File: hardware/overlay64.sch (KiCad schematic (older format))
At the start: 15 parts, among them IC1 ATMEGA8-P, P1 VIDEO IN, P2 VIDEO OUT, Q1 PNP, U1 LM1881, Y1 14.7456MHz

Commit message: Hardware: Schematics switched to 1284P including USB, still drafting...
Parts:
- removed IC1: ATMEGA8-P, DIL28, symbol ATMEGA8-P
- removed Q1: PNP, symbol Q_PNP_BCE
- removed R1: 4k7, symbol R_Small
- removed RV1: 1K, symbol POT
- added D1, D2: 3.6V, symbol ZENERsmall
- added IC1: ATMEGA1284-P, DIL40, symbol ATMEGA1284-P
- added P3: CHROMA IN, symbol CONN_01X02
- added P4: USB, symbol CONN_01X05
- added P5: CHROMA OUT, symbol CONN_01X02
- added P6: PORTA, symbol CONN_01X08
- added P7: PORTB, symbol CONN_01X08
- added P8: PORTC, symbol CONN_01X08
- added Q? (x2): NPN, symbol Q_NPN_BCE
- added R1, R3: 1k, symbol R
- added R4: 1k5, symbol R
- added R5, R6: 68, symbol R
- P1: value VIDEO IN -> LUMA IN
- P2: value VIDEO OUT -> LUMA OUT
- Y1: value 14.7456MHz -> 16MHz
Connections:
- net labels added: LUMA, OUT, PA0, PA1, PA2, PA3, PA4, PA5, PA6, PA7, PB0, PB1, PB2, PB3, PB4, PB5, PB6, PB7, PC0, PC1, PC2, PC3, PC4, PC5, PC6, PC7
- wire segments 26 -> 22
- no-connect marks 18 -> 8
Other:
- moved on the sheet: C3, C5, C6, R2, U1, Y1

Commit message: Hardware: Switched to atmega32p, updated to current state on breadboard
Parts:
- removed C1, C2: 18pF, symbol CP_Small
- removed D1, D2: 3.6V, symbol ZENERsmall
- removed IC1: ATMEGA1284-P, DIL40, symbol ATMEGA1284-P
- removed P3: CHROMA IN, symbol CONN_01X02
- removed P4: USB, symbol CONN_01X05
- removed P5: CHROMA OUT, symbol CONN_01X02
- removed P6: PORTA, symbol CONN_01X08
- removed P7: PORTB, symbol CONN_01X08
- removed P8: PORTC, symbol CONN_01X08
- removed Q?: NPN, symbol Q_NPN_BCE
- removed R1, R3: 1k, symbol R
- removed R4: 1k5, symbol R
- removed R5, R6: 68, symbol R
- added C1, C2: 18pF, symbol C_Small
- added IC1: ATMEGA328P-P, DIL28, symbol ATMEGA328P-P
- added P1: ISP, symbol CONN_02X03
- added RV1: 1k, symbol POT
- gave numbers to parts that had none: 1
- renumbered C5 to C3, C3 to C5, P1 to P2, P2 to P3, R2 to R1
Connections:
- net labels added: MISO, MOSI, SCK, ~RESET
- net labels removed: LUMA, OUT, PA0, PA1, PA2, PA3, PA4, PA5, PA6, PA7, PB0, PB1, PB2, PB3, PB4, PB5, PB6, PB7, PC0, PC1, PC2, PC3, PC4, PC5, PC6, PC7
- no-connect marks 8 -> 19
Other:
- moved on the sheet: C3, C5, C6, Q1, R1, U1, Y1

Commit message: Hardware: Added vic sockets, layed out components (rough draft)
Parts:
- removed C4: 10uF, symbol CP
- removed P2: LUMA IN, symbol CONN_01X02
- removed P3: LUMA OUT, symbol CONN_01X02
- added C4: 100nF, Capacitors_ThroughHole:C_Disc_D3_P2.5, symbol C
- added P2: VIC IN, Housings_DIP:DIP-40_W15.24mm, symbol CONN_01X40
- added P3: VIC OUT, Housings_DIP:DIP-40_W15.24mm, symbol CONN_01X40
- C1, C2, C3, C5, C6: footprint (none) -> Capacitors_ThroughHole:C_Disc_D3_P2.5
- IC1: footprint DIL28 -> Housings_DIP:DIP-28_W7.62mm
- P1: footprint (none) -> Pin_Headers:Pin_Header_Straight_2x03
- Q1: footprint (none) -> TO_SOT_Packages_THT:TO-92_Inline_Narrow_Oval
- R1: footprint (none) -> Discret:R1
- RV1: footprint (none) -> Potentiometers:Potentiometer_Bourns_3339H_Angular_ScrewUp
- U1: footprint (none) -> Housings_DIP:DIP-8_W7.62mm
- Y1: footprint (none) -> Crystals:Crystal_HC49-U_Vertical
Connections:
- net labels added: LUMA
- wire segments 22 -> 62
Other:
- moved on the sheet: C1, C2, C3, C5, C6, IC1, P1, Q1, R1, RV1, U1, Y1

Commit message: Hardware: Removed VIC-Sockets and pcb layout
Designing this as a VIC-Adpater-board is too complicated, and maybe
not possible (depending on what the modulator still does to the signal
to make it a proper C/Y signal).

It's probably simpler to get LUMA from the connector internally.
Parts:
- removed P2: VIC IN, Housings_DIP:DIP-40_W15.24mm, symbol CONN_01X40
- removed P3: VIC OUT, Housings_DIP:DIP-40_W15.24mm, symbol CONN_01X40
- added P2: MAIN, Pin_Headers:Pin_Header_Straight_1x03, symbol CONN_01X03
- added P3: INPUT, Pin_Headers:Pin_Header_Straight_1x14, symbol CONN_01X14
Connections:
- net labels added: IN0, IN1, IN10, IN11, IN12, IN13, IN2, IN3, IN4, IN5, IN6, IN7, IN8, IN9
- net labels removed: LUMA
- wire segments 62 -> 25
- no-connect marks 19 -> 6
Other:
- moved on the sheet: C4

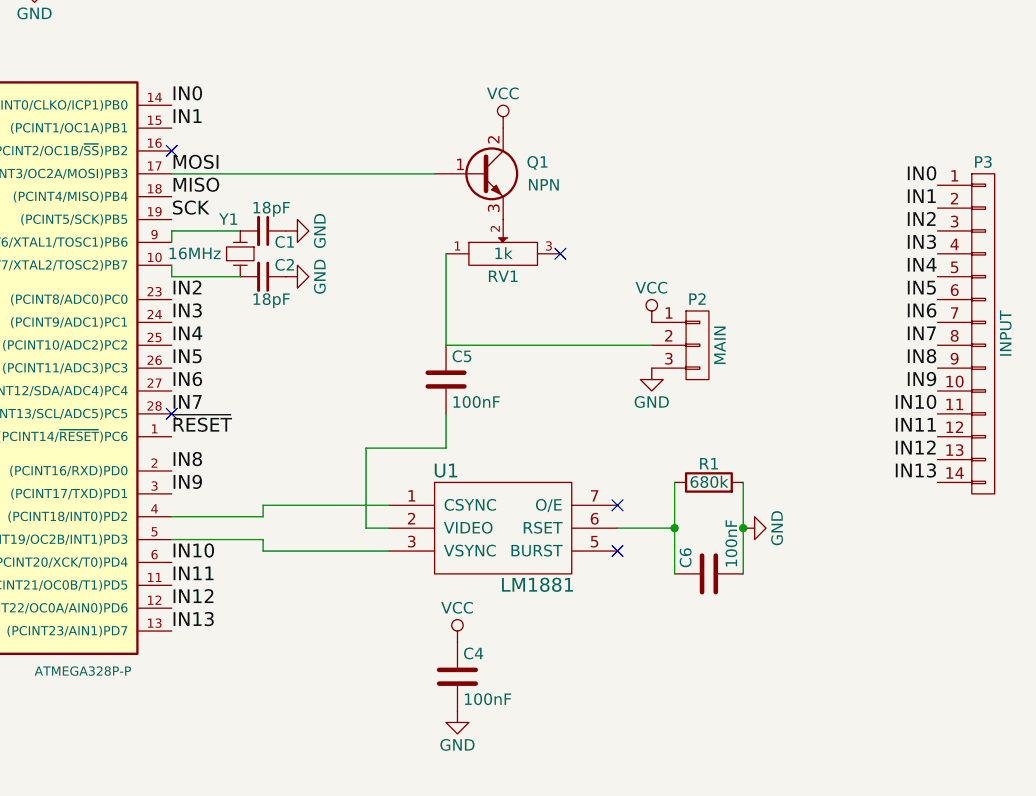
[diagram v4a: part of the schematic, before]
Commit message: Hardware: Updated schematics, Added /OE, resistor before transistor base
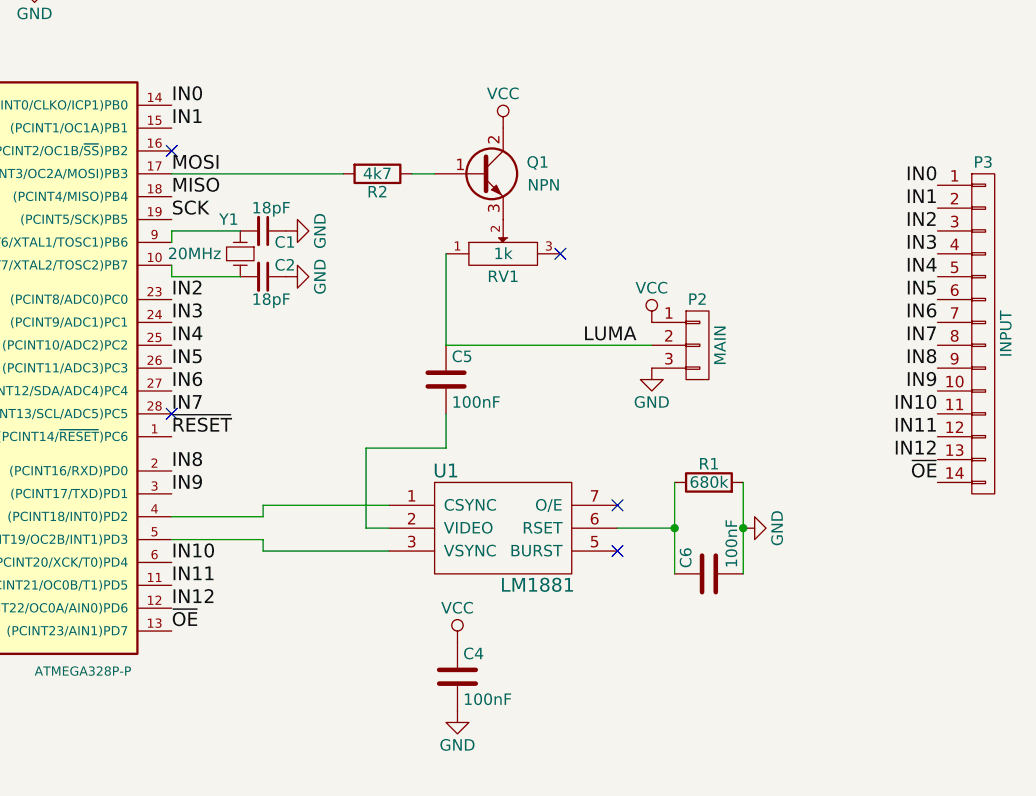
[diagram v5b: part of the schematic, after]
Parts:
- added R2: 4k7, symbol R
- Y1: value 16MHz -> 20MHz
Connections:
- net MOSI: now also R2.2; no longer Q1.1 (B)
- net LUMA: now reaches C5.1, P2.2 (P2), RV1.1
- net IN13 renamed ~OE
- new net: Q1.1 (B), R2.1
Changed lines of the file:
@@
 $EndComp
 $Comp
-L PWR_FLAG #FLG01
+L PWR_FLAG #FLG1
 U 1 1 56A1EF0B
 P 6250 7500
-F 0 "#FLG01" H 6250 7595 50  0001 C CNN
+F 0 "#FLG1" H 6250 7595 50  0001 C CNN
 F 1 "PWR_FLAG" H 6250 7680 50  0000 C CNN
 F 2 "" H 6250 7500 60  0000 C CNN
@@
 $EndComp
 $Comp
-L VCC #PWR02
+L VCC #PWR12
 U 1 1 56A1EF40
 P 6250 7500
-F 0 "#PWR02" H 6250 7350 50  0001 C CNN
+F 0 "#PWR12" H 6250 7350 50  0001 C CNN
 F 1 "VCC" H 6250 7650 50  0000 C CNN
 F 2 "" H 6250 7500 60  0000 C CNN
@@
 $EndComp
 $Comp
-L PWR_FLAG #FLG03
+L PWR_FLAG #FLG2
 U 1 1 56A1EF56
 P 6700 7500
-F 0 "#FLG03" H 6700 7595 50  0001 C CNN
+F 0 "#FLG2" H 6700 7595 50  0001 C CNN
 F 1 "PWR_FLAG" H 6700 7680 50  0000 C CNN
 F 2 "" H 6700 7500 60  0000 C CNN
@@
 $EndComp
 $Comp
-L GND #PWR04
+L GND #PWR15
 U 1 1 56A1EF6C
 P 6700 7500
-F 0 "#PWR04" H 6700 7250 50  0001 C CNN
+F 0 "#PWR15" H 6700 7250 50  0001 C CNN
 F 1 "GND" H 6700 7350 50  0000 C CNN
 F 2 "" H 6700 7500 60  0000 C CNN
@@
 $EndComp
 $Comp
-L VCC #PWR05
+L VCC #PWR9
 U 1 1 56A1F13D
 P 5600 4850
-F 0 "#PWR05" H 5600 4700 50  0001 C CNN
+F 0 "#PWR9" H 5600 4700 50  0001 C CNN
 F 1 "VCC" H 5600 5000 50  0000 C CNN
 F 2 "" H 5600 4850 60  0000 C CNN
@@
 $EndComp
 $Comp
-L GND #PWR06
+L GND #PWR10
 U 1 1 56A1F155
 P 5600 5150
-F 0 "#PWR06" H 5600 4900 50  0001 C CNN
+F 0 "#PWR10" H 5600 4900 50  0001 C CNN
 F 1 "GND" H 5600 5000 50  0000 C CNN
 F 2 "" H 5600 5150 60  0000 C CNN
@@
 $EndComp
 $Comp
-L GND #PWR07
+L GND #PWR2
 U 1 1 56A1F1BC
 P 2050 2800
-F 0 "#PWR07" H 2050 2550 50  0001 C CNN
+F 0 "#PWR2" H 2050 2550 50  0001 C CNN
 F 1 "GND" H 2050 2650 50  0000 C CNN
 F 2 "" H 2050 2800 60  0000 C CNN
@@
 $EndComp
 $Comp
-L GND #PWR08
+L GND #PWR16
 U 1 1 56A1F3BB
 P 6850 4350
-F 0 "#PWR08" H 6850 4100 50  0001 C CNN
+F 0 "#PWR16" H 6850 4100 50  0001 C CNN
 F 1 "GND" H 6850 4200 50  0000 C CNN
 F 2 "" H 6850 4350 60  0000 C CNN
@@
 P 4650 3150
 F 0 "Y1" V 4500 3200 50  0000 C CNN
-F 1 "16MHz" V 4650 3350 50  0000 C CNN
+F 1 "20MHz" V 4650 3350 50  0000 C CNN
 F 2 "Crystals:Crystal_HC49-U_Vertical" H 4650 3150 60  0001 C CNN
 F 3 "" H 4650 3150 60  0000 C CNN
@@
 $EndComp
 $Comp
-L VCC #PWR09
+L VCC #PWR1
 U 1 1 56A1FF3A
 P 2000 2500
-F 0 "#PWR09" H 2000 2350 50  0001 C CNN
+F 0 "#PWR1" H 2000 2350 50  0001 C CNN
 F 1 "VCC" H 2000 2650 50  0000 C CNN
 F 2 "" H 2000 2500 60  0000 C CNN
@@
 $EndComp
 $Comp
-L GND #PWR010
+L GND #PWR3
 U 1 1 56A20155
 P 2450 4700
-F 0 "#PWR010" H 2450 4450 50  0001 C CNN
+F 0 "#PWR3" H 2450 4450 50  0001 C CNN
 F 1 "GND" H 2450 4550 50  0000 C CNN
 F 2 "" H 2450 4700 60  0000 C CNN
@@
 $EndComp
 $Comp
-L GND #PWR011
+L GND #PWR4
 U 1 1 56A60DBD
 P 2450 4800
-F 0 "#PWR011" H 2450 4550 50  0001 C CNN
+F 0 "#PWR4" H 2450 4550 50  0001 C CNN
 F 1 "GND" H 2450 4650 50  0000 C CNN
 F 2 "" H 2450 4800 60  0000 C CNN
@@
 $EndComp
 $Comp
-L VCC #PWR012
+L VCC #PWR11
 U 1 1 56A78618
 P 5800 2600
-F 0 "#PWR012" H 5800 2450 50  0001 C CNN
+F 0 "#PWR11" H 5800 2450 50  0001 C CNN
 F 1 "VCC" H 5800 2750 50  0000 C CNN
 F 2 "" H 5800 2600 60  0000 C CNN
@@
 MOSI
 $Comp
-L VCC #PWR013
+L VCC #PWR5
 U 1 1 56A92B5A
 P 3750 1750
-F 0 "#PWR013" H 3750 1600 50  0001 C CNN
+F 0 "#PWR5" H 3750 1600 50  0001 C CNN
 F 1 "VCC" H 3750 1900 50  0000 C CNN
 F 2 "" H 3750 1750 60  0000 C CNN
@@
 $EndComp
 $Comp
-L GND #PWR014
+L GND #PWR6
 U 1 1 56A92BBD
 P 3750 1950
-F 0 "#PWR014" H 3750 1700 50  0001 C CNN
+F 0 "#PWR6" H 3750 1700 50  0001 C CNN
 F 1 "GND" H 3750 1800 50  0000 C CNN
 F 2 "" H 3750 1950 60  0000 C CNN
@@
 $EndComp
 $Comp
-L GND #PWR015
+L GND #PWR7
 U 1 1 56A976F1
 P 4850 3050
-F 0 "#PWR015" H 4850 2800 50  0001 C CNN
+F 0 "#PWR7" H 4850 2800 50  0001 C CNN
 F 1 "GND" H 4850 2900 50  0000 C CNN
 F 2 "" H 4850 3050 60  0000 C CNN
@@
 $EndComp
 $Comp
-L GND #PWR016
+L GND #PWR8
 U 1 1 56A97733
 P 4850 3250
-F 0 "#PWR016" H 4850 3000 50  0001 C CNN
+F 0 "#PWR8" H 4850 3000 50  0001 C CNN
 F 1 "GND" H 4850 3100 50  0000 C CNN
 F 2 "" H 4850 3250 60  0000 C CNN
@@
 NoConn ~ 4350 3850
 NoConn ~ 4350 2700
-Wire Wire Line
-	5500 2800 4350 2800
 Wire Wire Line
 	5550 3150 5550 3550
@@
 $EndComp
 $Comp
-L VCC #PWR017
+L VCC #PWR13
 U 1 1 56A9E7D0
 P 6450 3450
-F 0 "#PWR017" H 6450 3300 50  0001 C CNN
+F 0 "#PWR13" H 6450 3300 50  0001 C CNN
 F 1 "VCC" H 6450 3600 50  0000 C CNN
 F 2 "" H 6450 3450 60  0000 C CNN
@@
 $EndComp
 $Comp
-L GND #PWR018
+L GND #PWR14
 U 1 1 56A9E875
 P 6450 3650
-F 0 "#PWR018" H 6450 3400 50  0001 C CNN
+F 0 "#PWR14" H 6450 3400 50  0001 C CNN
 F 1 "GND" H 6450 3500 50  0000 C CNN
 F 2 "" H 6450 3650 60  0000 C CNN
@@
 Text Label 4350 4700 0    60   ~ 0
 IN12
-Text Label 4350 4800 0    60   ~ 0
-IN13
 Wire Wire Line
 	5300 4350 5200 4350
@@
 Text Label 7700 4050 2    60   ~ 0
 IN12
+$Comp
+L R R2
+U 1 1 56AA9AFF
+P 5250 2800
+F 0 "R2" V 5330 2800 50  0000 C CNN
+F 1 "4k7" V 5250 2800 50  0000 C CNN
+F 2 "" V 5180 2800 50  0000 C CNN
+F 3 "" H 5250 2800 50  0000 C CNN
+	1    5250 2800
+	0    1    1    0
+$EndComp
+Wire Wire Line
+	4350 2800 5100 2800
+Wire Wire Line
+	5400 2800 5500 2800
+Text Label 4350 4800 0    60   ~ 0
+~OE
 Text Label 7700 4150 2    60   ~ 0
-IN13
+~OE
+Text Label 6150 3550 0    60   ~ 0
+LUMA
 $EndSCHEMATC

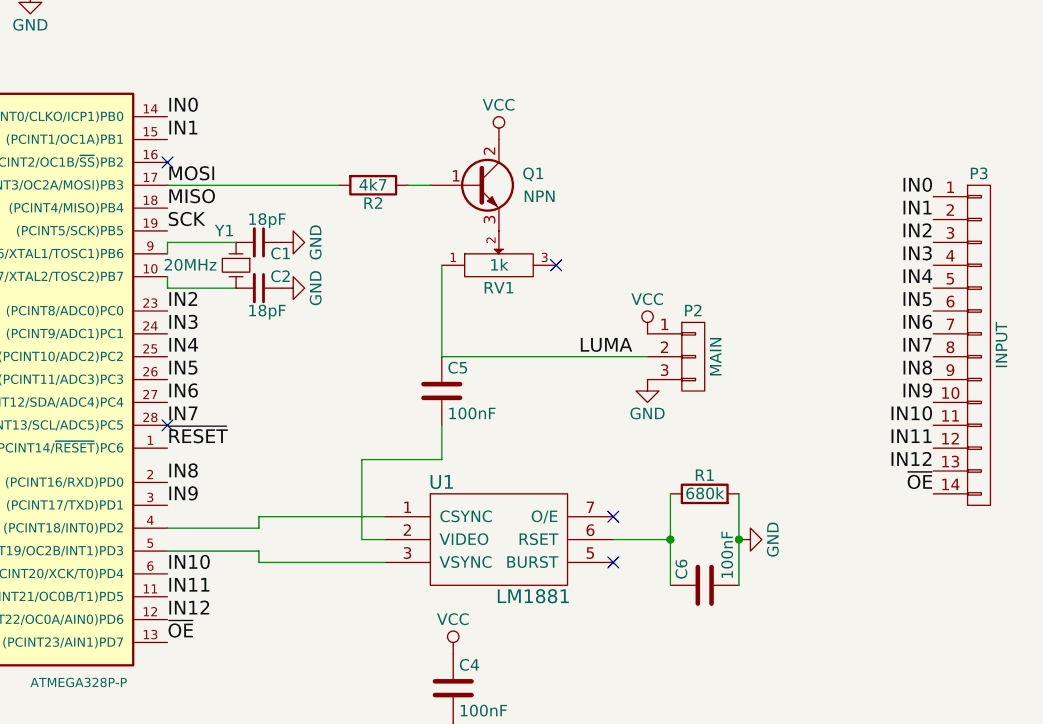
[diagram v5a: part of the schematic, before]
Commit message: Hardware: Removed wrong "no connection" symbol on IN7
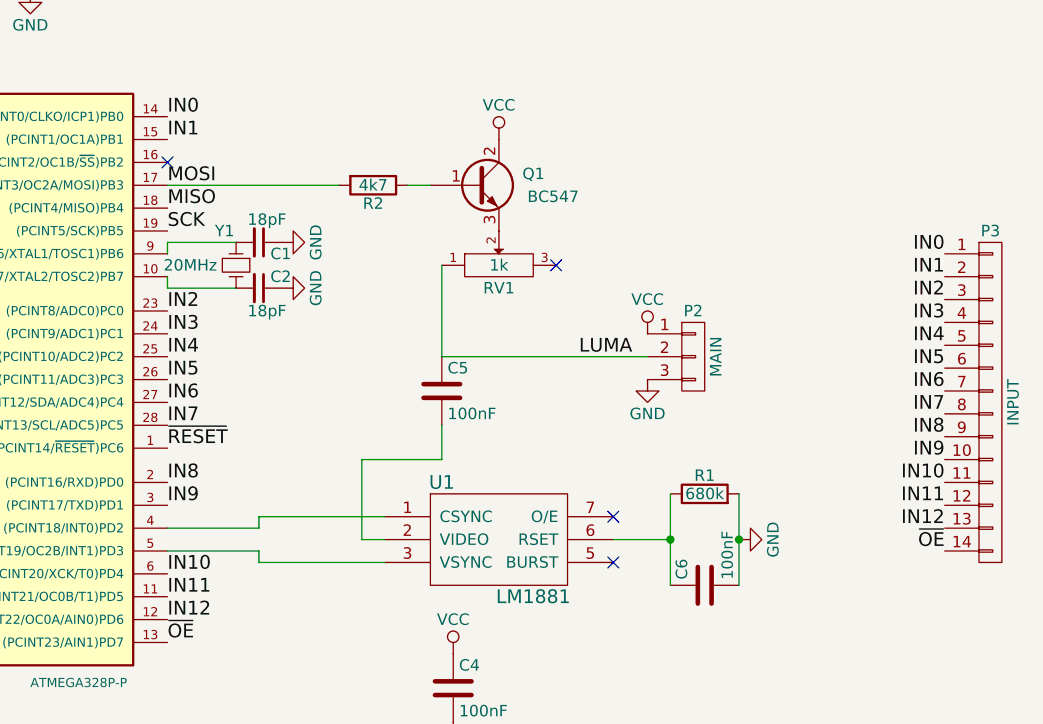
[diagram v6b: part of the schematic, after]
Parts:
- Q1: value NPN -> BC547
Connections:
- no-connect marks 6 -> 5
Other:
- moved on the sheet: P3
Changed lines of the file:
@@
 encoding utf-8
 Sheet 1 1
-Title ""
-Date ""
-Rev ""
-Comp ""
-Comment1 ""
+Title "Simple Video Overlay Driver"
+Date "2016-02-02"
+Rev "1"
+Comp "Henning Bekel"
+Comment1 "http://www.henning-bekel.de"
 Comment2 ""
 Comment3 ""
@@
 P 5700 2800
 F 0 "Q1" H 6000 2850 50  0000 R CNN
-F 1 "NPN" H 6050 2750 50  0000 R CNN
+F 1 "BC547" H 6150 2750 50  0000 R CNN
 F 2 "TO_SOT_Packages_THT:TO-92_Inline_Narrow_Oval" H 5900 2900 29  0001 C CNN
 F 3 "" H 5700 2800 60  0000 C CNN
@@
 Wire Wire Line
 	4350 3250 4350 3200
-NoConn ~ 4350 3850
 NoConn ~ 4350 2700
 Wire Wire Line
@@
 L CONN_01X14 P3
 U 1 1 56A9F1EA
-P 7900 3500
-F 0 "P3" H 7900 4250 50  0000 C CNN
-F 1 "INPUT" V 8000 3500 50  0000 C CNN
-F 2 "Pin_Headers:Pin_Header_Straight_1x14" H 7900 3500 60  0001 C CNN
-F 3 "" H 7900 3500 60  0000 C CNN
-	1    7900 3500
-	1    0    0    -1
-$EndComp
-Text Label 7700 2850 2    60   ~ 0
+P 7950 3750
+F 0 "P3" H 7950 4500 50  0000 C CNN
+F 1 "INPUT" V 8050 3750 50  0000 C CNN
+F 2 "Pin_Headers:Pin_Header_Straight_1x14" H 7950 3750 60  0001 C CNN
+F 3 "" H 7950 3750 60  0000 C CNN
+	1    7950 3750
+	1    0    0    -1
+$EndComp
+Text Label 7750 3100 2    60   ~ 0
 IN0
-Text Label 7700 2950 2    60   ~ 0
+Text Label 7750 3200 2    60   ~ 0
 IN1
-Text Label 7700 3050 2    60   ~ 0
+Text Label 7750 3300 2    60   ~ 0
 IN2
-Text Label 7700 3150 2    60   ~ 0
+Text Label 7750 3400 2    60   ~ 0
 IN3
-Text Label 7700 3250 2    60   ~ 0
+Text Label 7750 3500 2    60   ~ 0
 IN4
-Text Label 7700 3350 2    60   ~ 0
+Text Label 7750 3600 2    60   ~ 0
 IN5
-Text Label 7700 3450 2    60   ~ 0
+Text Label 7750 3700 2    60   ~ 0
 IN6
-Text Label 7700 3550 2    60   ~ 0
+Text Label 7750 3800 2    60   ~ 0
 IN7
-Text Label 7700 3650 2    60   ~ 0
+Text Label 7750 3900 2    60   ~ 0
 IN8
-Text Label 7700 3750 2    60   ~ 0
+Text Label 7750 4000 2    60   ~ 0
 IN9
-Text Label 7700 3850 2    60   ~ 0
+Text Label 7750 4100 2    60   ~ 0
 IN10
-Text Label 7700 3950 2    60   ~ 0
+Text Label 7750 4200 2    60   ~ 0
 IN11
-Text Label 7700 4050 2    60   ~ 0
+Text Label 7750 4300 2    60   ~ 0
 IN12
 $Comp
@@
 Text Label 4350 4800 0    60   ~ 0
 ~OE
-Text Label 7700 4150 2    60   ~ 0
+Text Label 7750 4400 2    60   ~ 0
 ~OE
 Text Label 6150 3550 0    60   ~ 0
